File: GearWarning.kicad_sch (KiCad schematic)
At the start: 5 parts

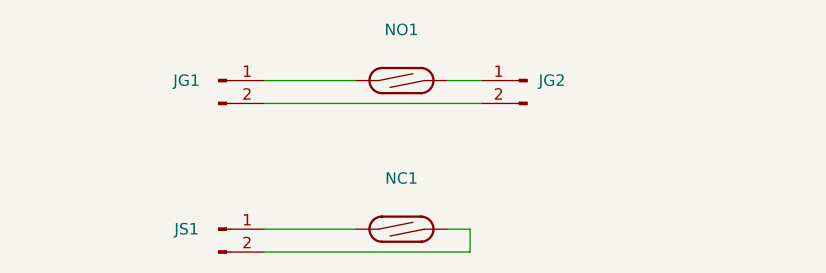
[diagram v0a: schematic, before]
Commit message: added circuit diagram to schematic
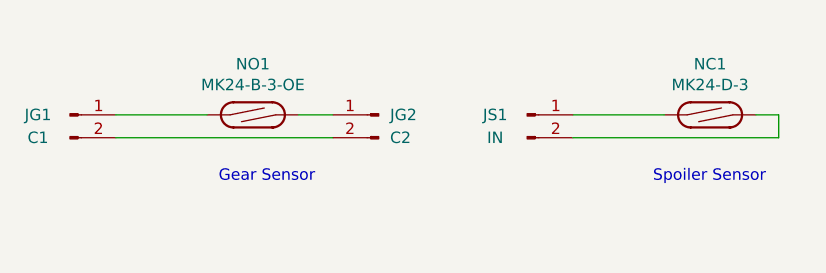
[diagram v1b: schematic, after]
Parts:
- JG1: value (none) -> C1; footprint (none) -> Connector_JST:JST_PH_S2B-PH-K_1x02_P2.00mm_Horizontal
- JG2: value (none) -> C2; footprint (none) -> Connector_JST:JST_PH_S2B-PH-K_1x02_P2.00mm_Horizontal
- JS1: value (none) -> IN; footprint (none) -> Connector_JST:JST_PH_S2B-PH-K_1x02_P2.00mm_Horizontal
- NC1: value (none) -> MK24-D-3
- NO1: value (none) -> MK24-B-3-OE
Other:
- note added: "Gear Sensor"
- note added: "Spoiler Sensor"
- moved on the sheet: JG1, JG2, JS1, NC1, NO1
